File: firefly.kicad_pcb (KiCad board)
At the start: 2 copper layers, 21.6 x 80.6 mm, 39 parts, among them J1 Barrel_Jack, J2 Conn_01x14, J3 Conn_01x14, J4 Conn_01x02, J5 Conn_01x04, J6 Power_Jumper, J7 Conn_01x06, J8 Conn_02x03_Odd_Even, SW1 SW_Push, U1 NCP1117-5.0_SOT223, U2 ATmega328P-PU, U3 LP2985-3.3, U4 LMV321, Y1 16 MHz

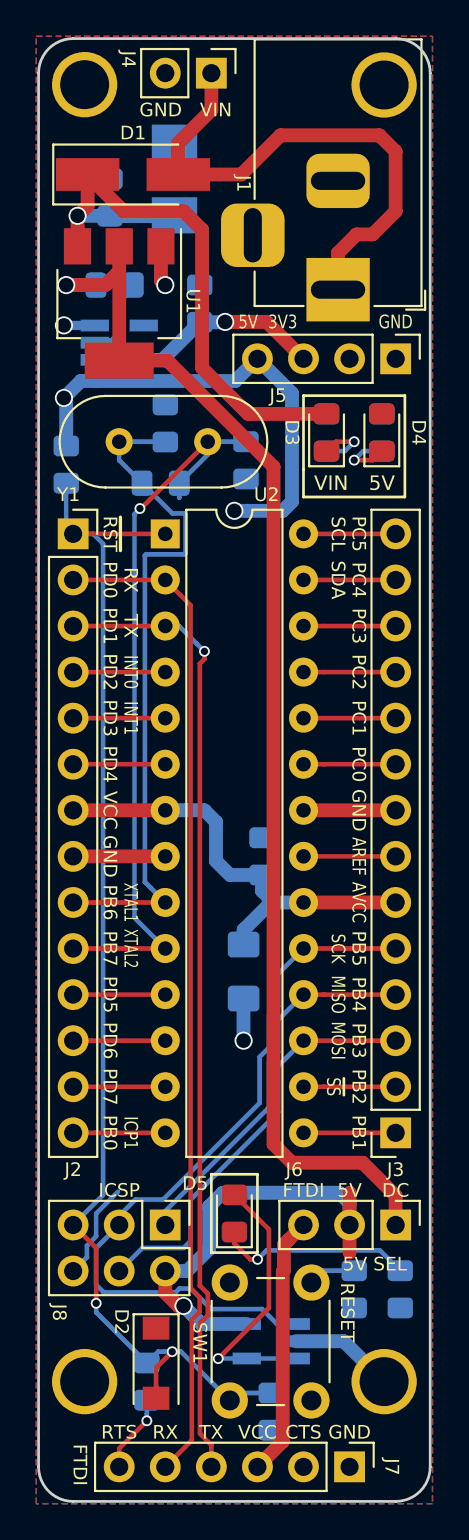
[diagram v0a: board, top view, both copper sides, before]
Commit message: Moved some components and silkscreen around, replaced crystal.
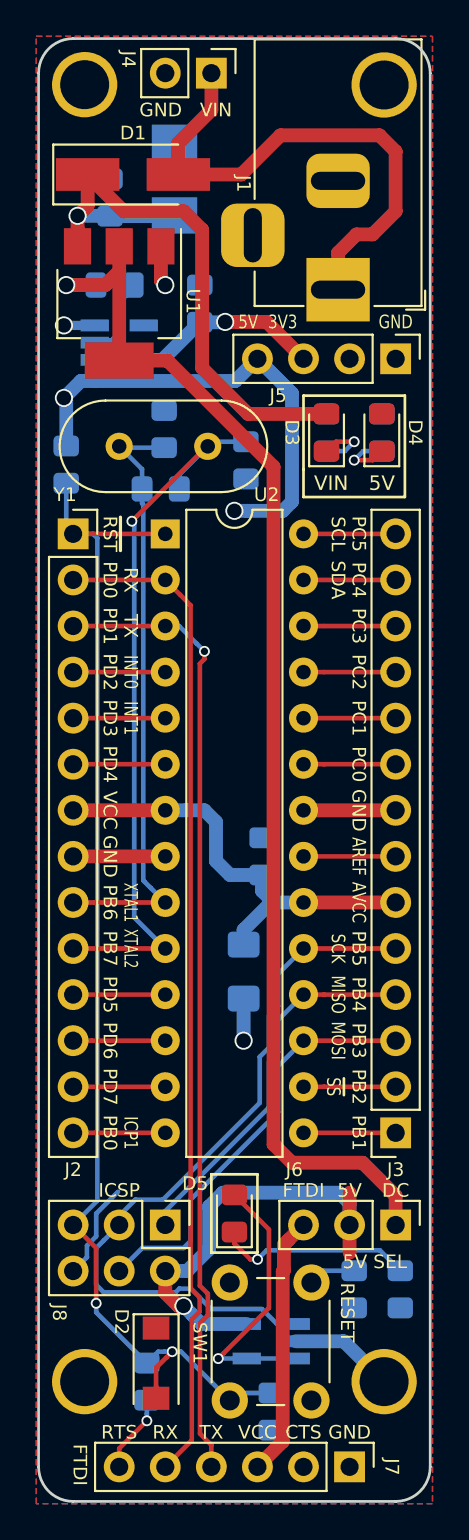
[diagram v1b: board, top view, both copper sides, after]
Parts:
- moved R1 0.32 mm to (146.8, 89.0)
- moved C6 0.31 mm to (147.0, 85.7)
- moved Y1 0.25 mm to (144.5, 86.6)
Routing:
- net /OSC1: track 37.6 -> 33.8 mm
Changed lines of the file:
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@@
     (thickness 1.6)
     (drawings 82)
-    (tracks 297)
+    (tracks 296)
     (zones 0)
     (modules 39)
@@
   (title_block
     (title "FireFly v1")
-    (date 2018-09-25)
+    (date 2018-09-26)
     (rev A)
     (comment 2 "California Institute of Technology")
@@
     (tags "capacitor handsolder")
     (attr smd)
-    (fp_text reference C3 (at 1.016 -1.397 90) (layer B.SilkS)
+    (fp_text reference C3 (at 1.016 -1.524 90) (layer B.SilkS)
       (effects (font (size 0.75 0.75) (thickness 0.1)) (justify mirror))
     )
@@
   )
   (module Capacitor_SMD:C_0805_2012Metric_Pad1.15x1.40mm_HandSolder (layer B.Cu)
-    (at 147.066 85.353 90)
+    (at 147.0025 85.6615 90)
     (descr "Capacitor SMD 0805 (2012 Metric), square (rectangular) end terminal, IPC_7351 nominal with elongated pad for handsoldering. (Body size source: https://docs.google.com/spreadsheets/d/1BsfQQcO9C6DZCsRaXUlFlo91Tg2WpOkGARC1WS5S8t0/edit?usp=sharing), generated with kicad-footprint-generator")
     (tags "capacitor handsolder")
@@
     (tags "LED handsolder")
     (attr smd)
-    (fp_text reference D4 (at 0 2.032 270 unlocked) (layer F.SilkS)
+    (fp_text reference D4 (at 0 1.8415 270 unlocked) (layer F.SilkS)
       (effects (font (size 0.75 0.75) (thickness 0.1)))
     )
@@
   )
   (module Resistor_SMD:R_0805_2012Metric_Pad1.15x1.40mm_HandSolder (layer B.Cu)
-    (at 146.812 88.646)
+    (at 146.812 88.9635)
     (descr "Resistor SMD 0805 (2012 Metric), square (rectangular) end terminal, IPC_7351 nominal with elongated pad for handsoldering. (Body size source: https://docs.google.com/spreadsheets/d/1BsfQQcO9C6DZCsRaXUlFlo91Tg2WpOkGARC1WS5S8t0/edit?usp=sharing), generated with kicad-footprint-generator")
     (tags "resistor handsolder")
     (attr smd)
-    (fp_text reference R1 (at 2.159 1.65) (layer B.SilkS)
+    (fp_text reference R1 (at 2.159 1.524) (layer B.SilkS)
       (effects (font (size 0.75 0.75) (thickness 0.1)) (justify mirror))
     )
@@
   )
   (module Crystal:Crystal_HC49-4H_Vertical (layer F.Cu)
-    (at 144.526 86.36)
+    (at 144.526 86.614)
     (descr "Crystal THT HC-49-4H http://5hertz.com/pdfs/04404_D.pdf")
     (tags "THT crystalHC-49-4H")
-    (fp_text reference Y1 (at -2.794 2.921) (layer F.SilkS)
+    (fp_text reference Y1 (at -2.9845 2.667) (layer F.SilkS)
       (effects (font (size 0.75 0.75) (thickness 0.1)))
     )
@@
     )
   )
-  (gr_text "5V SEL" (at 158.623 131.699) (layer F.SilkS)
+  (gr_text "5V SEL" (at 158.623 131.572) (layer F.SilkS)
     (effects (font (size 0.75 0.75) (thickness 0.1875)))
   )
@@
   (segment (start 143.188081 111.76) (end 147.066 111.76) (width 0.254) (layer F.Cu) (net 2))
   (segment (start 141.986 111.76) (end 143.188081 111.76) (width 0.254) (layer F.Cu) (net 2))
+  (segment (start 145.938999 110.632999) (end 146.266001 110.960001) (width 0.254) (layer B.Cu) (net 2))
+  (segment (start 146.266001 110.960001) (end 147.066 111.76) (width 0.254) (layer B.Cu) (net 2))
   (segment (start 147.048 86.36) (end 147.066 86.378) (width 0.254) (layer B.Cu) (net 2))
-  (segment (start 144.526 86.36) (end 147.048 86.36) (width 0.254) (layer B.Cu) (net 2))
-  (segment (start 144.526 87.385) (end 144.526 86.36) (width 0.254) (layer B.Cu) (net 2))
-  (segment (start 145.787 88.646) (end 144.526 87.385) (width 0.254) (layer B.Cu) (net 2))
-  (segment (start 148.127601 90.312999) (end 148.193001 90.378399) (width 0.254) (layer B.Cu) (net 2))
-  (segment (start 148.127601 92.567001) (end 146.004399 92.567001) (width 0.254) (layer B.Cu) (net 2))
-  (segment (start 146.004399 92.567001) (end 145.938999 92.632401) (width 0.254) (layer B.Cu) (net 2))
-  (segment (start 147.453999 90.312999) (end 148.127601 90.312999) (width 0.254) (layer B.Cu) (net 2))
-  (segment (start 148.193001 90.378399) (end 148.193001 92.501601) (width 0.254) (layer B.Cu) (net 2))
-  (segment (start 148.193001 92.501601) (end 148.127601 92.567001) (width 0.254) (layer B.Cu) (net 2))
-  (segment (start 145.938999 110.632999) (end 146.266001 110.960001) (width 0.254) (layer B.Cu) (net 2))
-  (segment (start 145.787 88.646) (end 147.453999 90.312999) (width 0.254) (layer B.Cu) (net 2))
-  (segment (start 146.266001 110.960001) (end 147.066 111.76) (width 0.254) (layer B.Cu) (net 2))
-  (segment (start 145.938999 92.632401) (end 145.938999 110.632999) (width 0.254) (layer B.Cu) (net 2))
+  (segment (start 145.787 87.875) (end 144.526 86.614) (width 0.254) (layer B.Cu) (net 2))
+  (segment (start 145.787 88.9635) (end 145.787 87.875) (width 0.254) (layer B.Cu) (net 2))
+  (segment (start 144.5985 86.6865) (end 144.526 86.614) (width 0.254) (layer B.Cu) (net 2))
+  (segment (start 147.0025 86.6865) (end 144.5985 86.6865) (width 0.254) (layer B.Cu) (net 2))
+  (segment (start 145.851502 110.545502) (end 145.923 110.617) (width 0.254) (layer B.Cu) (net 2))
+  (segment (start 145.851502 89.828002) (end 145.851502 110.545502) (width 0.254) (layer B.Cu) (net 2))
+  (segment (start 145.787 88.9635) (end 145.787 89.7635) (width 0.254) (layer B.Cu) (net 2))
+  (segment (start 145.787 89.7635) (end 145.851502 89.828002) (width 0.254) (layer B.Cu) (net 2))
   (segment (start 141.986 114.3) (end 147.066 114.3) (width 0.254) (layer F.Cu) (net 3))
-  (segment (start 149.406 86.36) (end 151.511 86.36) (width 0.254) (layer B.Cu) (net 3))
-  (segment (start 149.406 87.077) (end 149.406 86.36) (width 0.254) (layer B.Cu) (net 3))
-  (segment (start 147.837 88.646) (end 149.406 87.077) (width 0.254) (layer B.Cu) (net 3))
   (segment (start 147.837 89.446) (end 147.828 89.455) (width 0.254) (layer B.Cu) (net 3))
   (segment (start 147.837 88.646) (end 147.837 89.446) (width 0.254) (layer B.Cu) (net 3))
-  (segment (start 145.723 90.043) (end 145.668996 90.043) (width 0.254) (layer F.Cu) (net 3))
-  (via (at 145.668996 90.043) (size 0.6) (drill 0.4) (layers F.Cu B.Cu) (net 3))
-  (segment (start 147.066 114.3) (end 145.368997 112.602997) (width 0.254) (layer B.Cu) (net 3))
-  (segment (start 145.368997 90.342999) (end 145.668996 90.043) (width 0.254) (layer B.Cu) (net 3))
-  (segment (start 149.406 86.36) (end 145.723 90.043) (width 0.254) (layer F.Cu) (net 3))
-  (segment (start 145.368997 112.602997) (end 145.368997 90.342999) (width 0.254) (layer B.Cu) (net 3))
+  (segment (start 147.837 88.183) (end 147.837 88.9635) (width 0.254) (layer B.Cu) (net 3))
+  (segment (start 149.406 86.614) (end 147.837 88.183) (width 0.254) (layer B.Cu) (net 3))
+  (segment (start 149.66 86.36) (end 149.406 86.614) (width 0.254) (layer B.Cu) (net 3))
+  (segment (start 151.511 86.36) (end 149.66 86.36) (width 0.254) (layer B.Cu) (net 3))
+  (via (at 145.2245 90.7415) (size 0.6) (drill 0.4) (layers F.Cu B.Cu) (net 3))
+  (segment (start 149.352 86.614) (end 149.406 86.614) (width 0.254) (layer F.Cu) (net 3))
+  (segment (start 145.2245 90.7415) (end 149.352 86.614) (width 0.254) (layer F.Cu) (net 3))
+  (segment (start 145.161 90.805) (end 145.2245 90.7415) (width 0.254) (layer B.Cu) (net 3))
+  (segment (start 145.3515 90.8685) (end 145.2245 90.7415) (width 0.254) (layer B.Cu) (net 3))
+  (segment (start 147.066 114.3) (end 145.3515 112.5855) (width 0.254) (layer B.Cu) (net 3))
+  (segment (start 145.3515 112.5855) (end 145.3515 90.8685) (width 0.254) (layer B.Cu) (net 3))
   (segment (start 141.986 91.44) (end 143.09 91.44) (width 0.254) (layer F.Cu) (net 4))
   (segment (start 143.09 91.44) (end 147.066 91.44) (width 0.254) (layer F.Cu) (net 4))
-  (segment (start 141.986 129.54) (end 143.637 127.889) (width 0.254) (layer B.Cu) (net 4))
-  (segment (start 143.09 91.44) (end 141.986 91.44) (width 0.254) (layer B.Cu) (net 4))
-  (segment (start 143.637 91.987) (end 143.09 91.44) (width 0.254) (layer B.Cu) (net 4))
-  (segment (start 143.637 127.889) (end 143.637 91.987) (width 0.254) (layer B.Cu) (net 4))
   (segment (start 150.368 138.811) (end 150.622 139.065) (width 0.254) (layer F.Cu) (net 4))
   (segment (start 146.558 138.43) (end 146.558 138.587) (width 0.254) (layer F.Cu) (net 4))
@@
   (segment (start 141.605 91.059) (end 141.986 91.44) (width 0.254) (layer B.Cu) (net 4))
   (segment (start 141.605 88.646) (end 141.605 91.059) (width 0.254) (layer B.Cu) (net 4))
+  (segment (start 143.09 91.44) (end 141.986 91.44) (width 0.254) (layer B.Cu) (net 4))
+  (segment (start 143.3195 91.6695) (end 143.09 91.44) (width 0.254) (layer B.Cu) (net 4))
+  (segment (start 141.986 129.54) (end 143.3195 128.2065) (width 0.254) (layer B.Cu) (net 4))
+  (segment (start 143.3195 128.2065) (end 143.3195 91.6695) (width 0.254) (layer B.Cu) (net 4))
   (segment (start 146.05 139.954) (end 146.05 139.201) (width 0.254) (layer B.Cu) (net 5))
   (via (at 146.05 140.335) (size 0.6) (drill 0.4) (layers F.Cu B.Cu) (net 5))

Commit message: Add files for v1 release
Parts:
- removed the D2 at (146.6, 137.2)
- removed F1: 200mA, Fuse:Fuse_1206_3216Metric_Pad1.42x1.75mm_HandSolder
- removed U4: LMV321, Package_TO_SOT_SMD:SOT-23-5_HandSoldering
- added D1: CD1206-S01575, Diode_SMD:D_1206_3216Metric_Pad1.42x1.75mm_HandSolder, F.Cu at (147.1, 137.1)
- added G***: LOGO, w_logo:Logo_silk_polarity_center_5x1.4mm, B.Cu at (152.4, 68.8)
- added Q1: NTR5103, Package_TO_SOT_SMD:SOT-23_Handsoldering, B.Cu at (152.9, 135.9)
- added R6: 1K, Resistor_SMD:R_0805_2012Metric_Pad1.15x1.40mm_HandSolder, B.Cu at (147.2, 135.0)
- added REF**: OSHW-Logo_5.7x6mm_SilkScreen, Symbol:OSHW-Logo_5.7x6mm_SilkScreen, B.Cu at (150.9, 125.7)
- R4: renamed from R3; value 2K -> 1K
- R5: renamed from R4; value 10K -> 1K
- R7: renamed from R5; value 560 -> 330
- moved C5 1.89 mm to (147.8, 138.8)
- moved C4 0.13 mm to (152.9, 139.7)
- renumbered C3 to C1, C6 to C2, C7 to C3, C9 to C4, C8 to C5, C1 to C6, C4 to C7, C5 to C8, C2 to C9, D1 to D2, J4 to J2, J2 to J3, J6 to J4, J8 to J5, J7 to J6, J3 to J7, J5 to J8, R2 to R1, R1 to R2, R6 to R3, U3 to U2, U2 to U3
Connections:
- C9 pad 1: /P20 -> +5V
- D5 pad 2: Net-(D5-Pad2) -> +5V
- J1 pad 3: (no net) -> GND
- J3 pad 7: /P20 -> +5V
- J7 pad 6: /P20 -> +5V
- J8 pad 3: +3V3 -> +5V
- J8 pad 4: +5V -> +3V3
- R7 pad 2: GND -> Net-(Q1-Pad3)
- U2 pad 1: +5V -> /DC_5V
- U2 pad 3: +5V -> /DC_5V
- U3 pad 20: /P20 -> +5V
- U3 pad 7: /P20 -> +5V
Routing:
- net /P20: track 24.8 -> 0.00 mm
- net Net-(D5-Pad2): track 15.2 -> 0.00 mm, vias 1 -> 0
- net +5V: track 56.0 -> 69.0 mm, vias 5 -> 3
- net /P1: track 69.2 -> 79.6 mm, vias 2 -> 1
- net Net-(Q1-Pad3): track 0.00 -> 8.82 mm, vias 0 -> 2
- net /P19: track 41.3 -> 33.3 mm
- net /DC_5V: track 69.0 -> 76.7 mm
- net Net-(R3-Pad2): track 2.63 -> 10.0 mm
- net GND: track 28.2 -> 22.4 mm
- net Net-(Q1-Pad1): track 0.00 -> 3.96 mm
- net +3V3: track 10.5 -> 7.96 mm, vias 1 -> 0
- net /RTS#: track 4.31 -> 6.52 mm
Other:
- net class Default: via_dia 0.6 -> 0.762; via_drill 0.4 -> 0.381
- net class LED added: clearance 0.2, trace_width 0.381, via_dia 0.762, via_drill 0.381
- net class Power: via_dia 1 -> 1.143; via_drill 0.8 -> 0.635
